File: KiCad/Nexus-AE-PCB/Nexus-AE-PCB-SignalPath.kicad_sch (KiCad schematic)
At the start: 38 parts, among them J4 Inputs, J5 Outputs, U4 MCP6002T-I_MS, U5 MCP6002T-I_MS

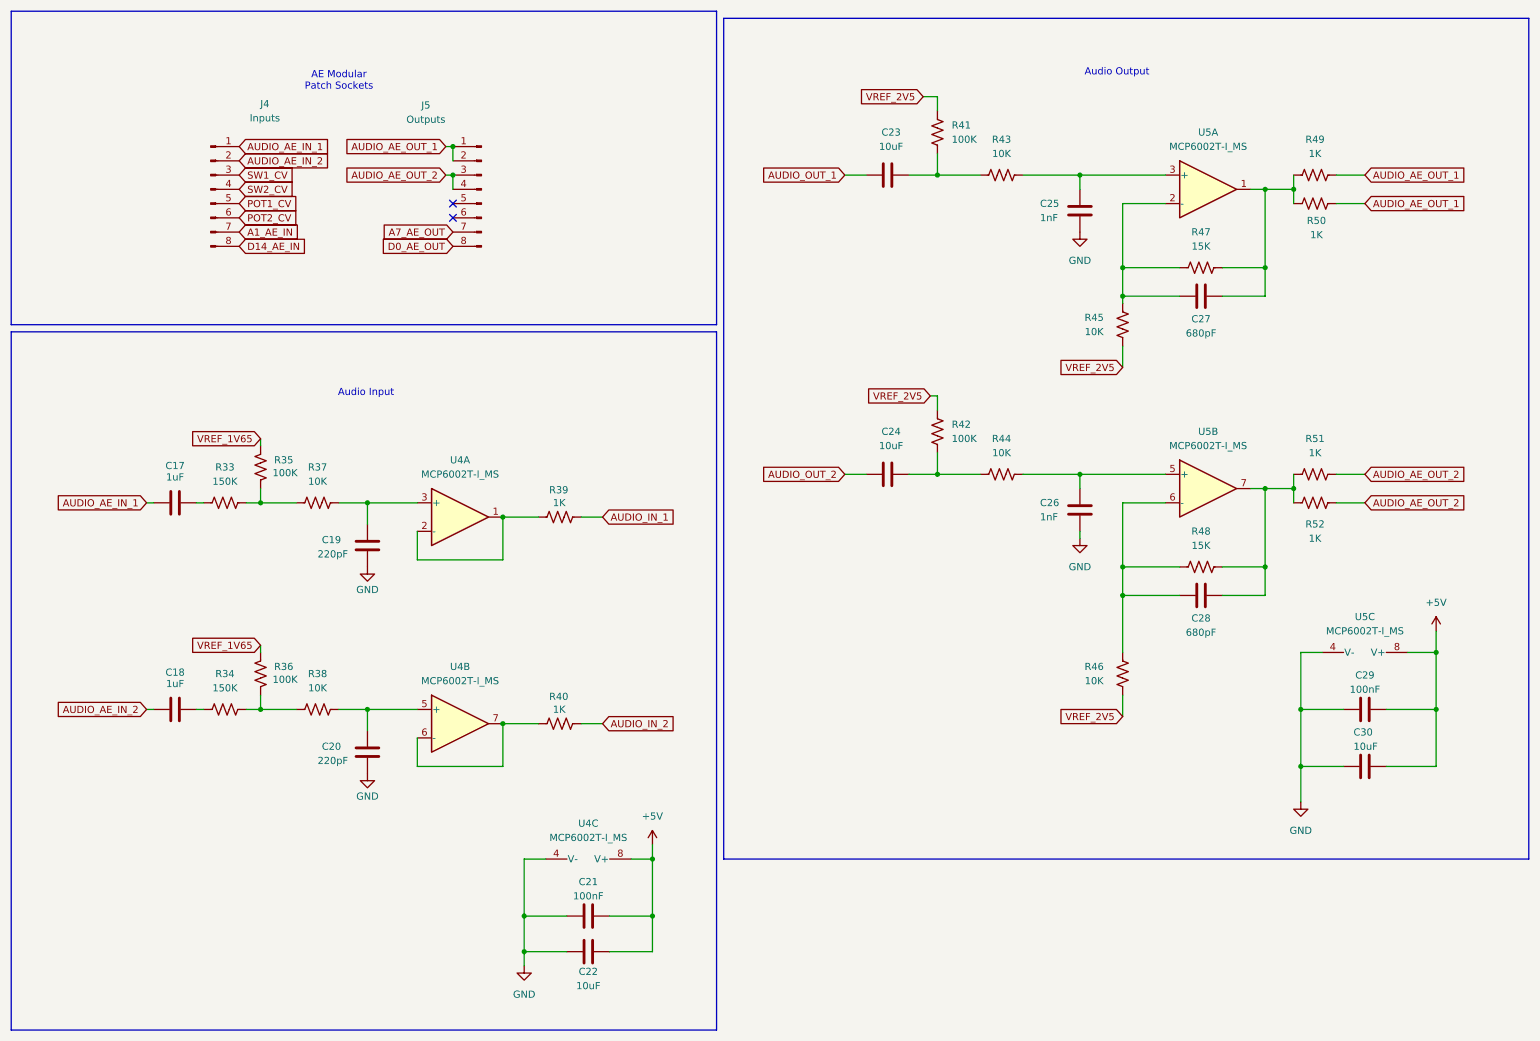
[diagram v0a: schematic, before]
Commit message: PCB and schmeatic are both approx 90% complete
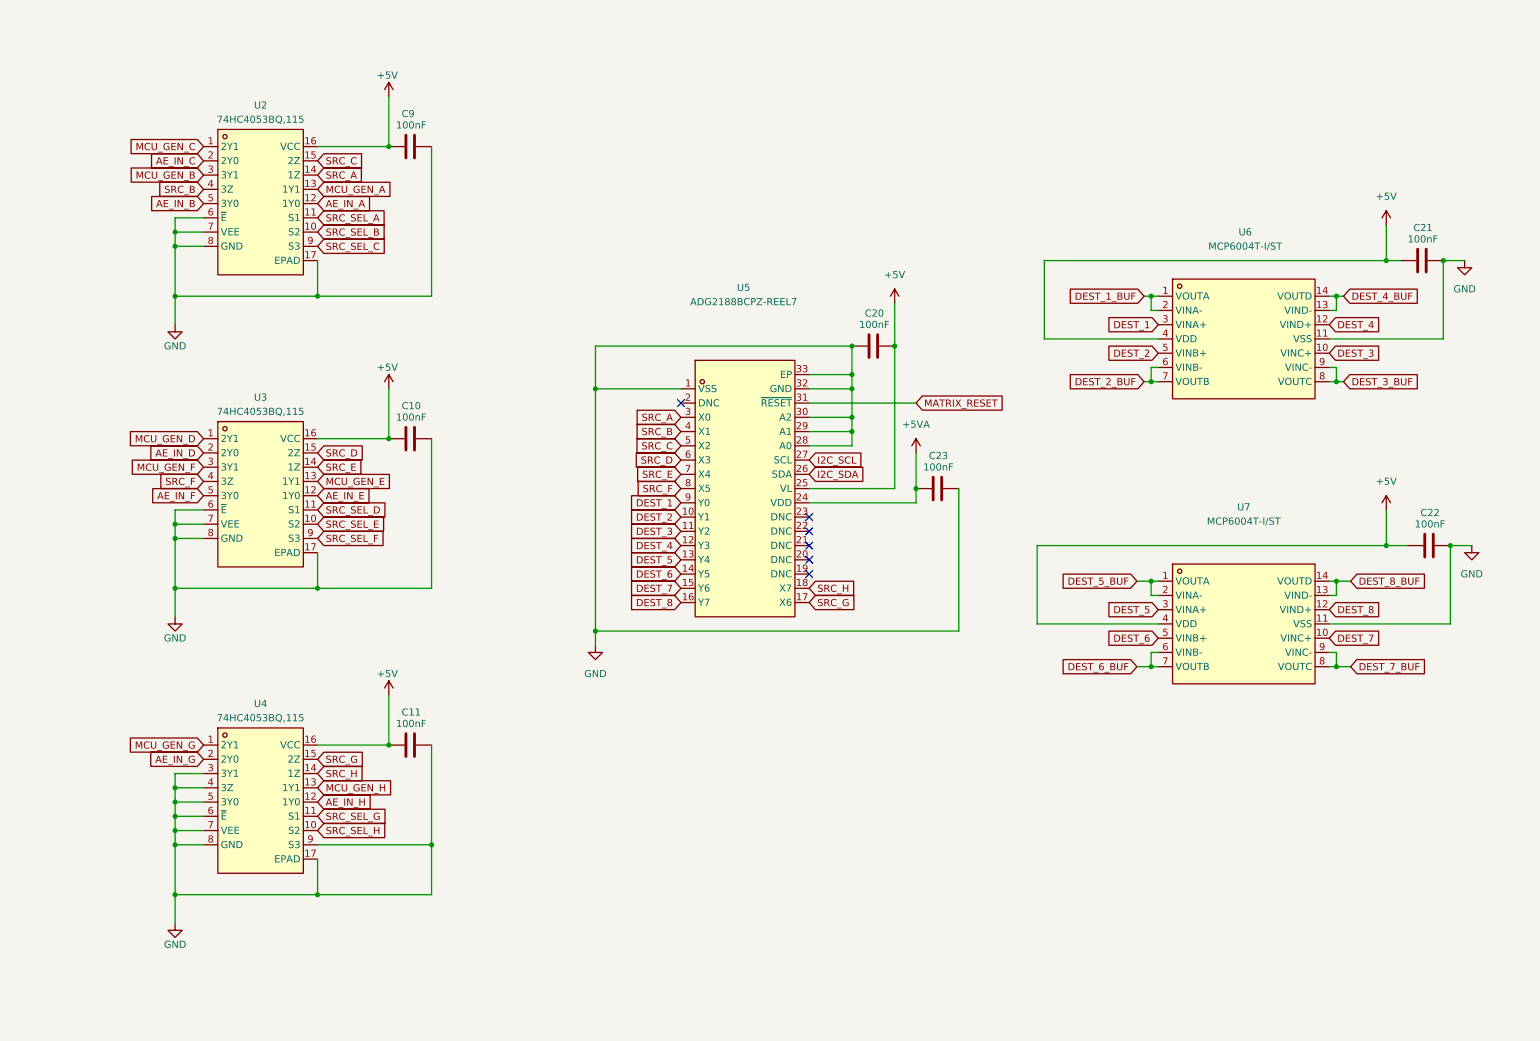
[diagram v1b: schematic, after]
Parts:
- removed C17, C18: 1uF, Capacitor_SMD:C_0603_1608Metric, symbol Device:C
- removed C19: 220pF, Capacitor_SMD:C_0603_1608Metric, symbol Device:C
- removed C24, C30: 10uF, Capacitor_SMD:C_0603_1608Metric, symbol Device:C
- removed C25, C26: 1nF, Capacitor_SMD:C_0603_1608Metric, symbol Device:C
- removed C27, C28: 680pF, Capacitor_SMD:C_0603_1608Metric, symbol Device:C
- removed C29: 100nF, Capacitor_SMD:C_0603_1608Metric, symbol Device:C
- removed J4: Inputs, clectric-diy:Connector_PinSocket-1x08-P2.54mm-H8.5mm_Preci-Dip_801-87-008-10-005101, symbol Connector:Conn_01x08_Pin
- removed J5: Outputs, clectric-diy:Connector_PinSocket-1x08-P2.54mm-H8.5mm_Preci-Dip_801-87-008-10-005101, symbol Connector:Conn_01x08_Pin
- removed R33, R34: 150K, Resistor_SMD:R_0603_1608Metric, symbol Device:R_US
- removed R35, R36, R41, R42: 100K, Resistor_SMD:R_0603_1608Metric, symbol Device:R_US
- removed R37, R38, R43, R44, R45, R46: 10K, Resistor_SMD:R_0603_1608Metric, symbol Device:R_US
- removed R39, R40, R49, R50, R51, R52: 1K, Resistor_SMD:R_0603_1608Metric, symbol Device:R_US
- removed R47, R48: 15K, Resistor_SMD:R_0603_1608Metric, symbol Device:R_US
- removed U4, U5: MCP6002T-I_MS, clectric-diy:Amplifier_Operational_Microchip_MCP6002T-I_MS, symbol Amplifier_Operational:MCP6002-xMS
- added C10, C11, C9: 100nF, Capacitor_SMD:C_0402_1005Metric, symbol Device:C
- added U2, U3, U4: 74HC4053BQ,115, clectric-diy:DHVQFN-16_L3.5-W2.5-P0.50-BL-EP, symbol clectric-diy:74HC4053BQ,115
- added U5: ADG2188BCPZ-REEL7, clectric-diy:LFCSP-32_L5.0-W5.0-P0.50-TL-EP3.1, symbol clectric-diy:ADG2188BCPZ-REEL7
- added U6, U7: MCP6004T-I/ST, clectric-diy:TSSOP-14_L5.0-W4.4-P0.65-LS6.4-BL, symbol clectric-diy:MCP6004T-I_ST
- C20: value 220pF -> 100nF; footprint Capacitor_SMD:C_0603_1608Metric -> Capacitor_SMD:C_0402_1005Metric
- C21: footprint Capacitor_SMD:C_0603_1608Metric -> Capacitor_SMD:C_0402_1005Metric
- C22, C23: value 10uF -> 100nF; footprint Capacitor_SMD:C_0603_1608Metric -> Capacitor_SMD:C_0402_1005Metric
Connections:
- net AUDIO_OUT_1 is gone; now on net GND: C23.2
- net +5V: now also C20.2, C21.1, C22.1, C10.1, C11.1, C9.1, U2.16 (VCC), U3.16 (VCC), U4.16 (VCC), U5.25 (VL), U6.4 (VDD), U7.4 (VDD); no longer C21.2, C22.2
- net GND: now also C20.1, C21.2, C22.2, C10.2, C11.2, C9.2, U2.17 (EPAD), U2.6 (~{E}), U2.7 (VEE), U2.8 (GND), U3.17 (EPAD), U3.6 (~{E}), U3.7 (VEE), U3.8 (GND), U4.17 (EPAD), U4.3 (3Y1), U4.4 (3Z), U4.5 (3Y0), U4.6 (~{E}), U4.7 (VEE), U4.8 (GND), U4.9 (S3), U5.1 (VSS), U5.28 (A0), U5.29 (A1), U5.30 (A2), U5.32 (GND), U5.33 (EP), U6.11 (VSS), U7.11 (VSS); no longer C20.2, C21.1, C22.1
- net +5VA: now reaches C23.1
- net +5VA: now also U5.24 (VDD)
- new net AE_IN_A: U2.12 (1Y0)
- new net AE_IN_B: U2.5 (3Y0)
- new net AE_IN_C: U2.2 (2Y0)
- new net AE_IN_D: U3.2 (2Y0)
- new net AE_IN_E: U3.12 (1Y0)
- new net AE_IN_F: U3.5 (3Y0)
- new net AE_IN_G: U4.2 (2Y0)
- new net AE_IN_H: U4.12 (1Y0)
- new net DEST_1: U5.9 (Y0), U6.3 (VINA+)
- new net DEST_1_BUF: U6.1 (VOUTA), U6.2 (VINA-)
- new net DEST_2: U5.10 (Y1), U6.5 (VINB+)
- new net DEST_2_BUF: U6.6 (VINB-), U6.7 (VOUTB)
- new net DEST_3: U5.11 (Y2), U6.10 (VINC+)
- new net DEST_3_BUF: U6.8 (VOUTC), U6.9 (VINC-)
- new net DEST_4: U5.12 (Y3), U6.12 (VIND+)
- new net DEST_4_BUF: U6.13 (VIND-), U6.14 (VOUTD)
- new net DEST_5: U5.13 (Y4), U7.3 (VINA+)
- new net DEST_5_BUF: U7.1 (VOUTA), U7.2 (VINA-)
- new net DEST_6: U5.14 (Y5), U7.5 (VINB+)
- new net DEST_6_BUF: U7.6 (VINB-), U7.7 (VOUTB)
- new net DEST_7: U5.15 (Y6), U7.10 (VINC+)
- new net DEST_7_BUF: U7.8 (VOUTC), U7.9 (VINC-)
- new net DEST_8: U5.16 (Y7), U7.12 (VIND+)
- new net DEST_8_BUF: U7.13 (VIND-), U7.14 (VOUTD)
- new net I2C_SCL: U5.27 (SCL)
- new net I2C_SDA: U5.26 (SDA)
- new net MATRIX_RESET: U5.31 (~{RESET})
- new net MCU_GEN_A: U2.13 (1Y1)
- new net MCU_GEN_B: U2.3 (3Y1)
- new net MCU_GEN_C: U2.1 (2Y1)
- new net MCU_GEN_D: U3.1 (2Y1)
- new net MCU_GEN_E: U3.13 (1Y1)
- new net MCU_GEN_F: U3.3 (3Y1)
- new net MCU_GEN_G: U4.1 (2Y1)
- new net MCU_GEN_H: U4.13 (1Y1)
- new net SRC_A: U2.14 (1Z), U5.3 (X0)
- new net SRC_B: U2.4 (3Z), U5.4 (X1)
- new net SRC_C: U2.15 (2Z), U5.5 (X2)
- new net SRC_D: U3.15 (2Z), U5.6 (X3)
- new net SRC_E: U3.14 (1Z), U5.7 (X4)
- new net SRC_F: U3.4 (3Z), U5.8 (X5)
- new net SRC_G: U4.15 (2Z), U5.17 (X6)
- new net SRC_H: U4.14 (1Z), U5.18 (X7)
- new net SRC_SEL_A: U2.11 (S1)
- new net SRC_SEL_B: U2.10 (S2)
- new net SRC_SEL_C: U2.9 (S3)
- new net SRC_SEL_D: U3.11 (S1)
- new net SRC_SEL_E: U3.10 (S2)
- new net SRC_SEL_F: U3.9 (S3)
- new net SRC_SEL_G: U4.11 (S1)
- new net SRC_SEL_H: U4.10 (S2)
- no-connect marks 2 -> 6
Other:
- note removed: "AE Modular Patch Sockets"
- note removed: "Audio Input"
- note removed: "Audio Output"
